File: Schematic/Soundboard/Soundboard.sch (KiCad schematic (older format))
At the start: 0 parts

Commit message: Begin rev 2 part selection and schematic
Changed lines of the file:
@@
 $Descr A4 11693 8268
 encoding utf-8
-Sheet 1 4
+Sheet 1 6
 Title ""
 Date ""
@@
 $EndSheet
 $Sheet
-S 4000 3200 1200 850
+S 4000 3050 1200 850
 U 5F0E4BAF
 F0 "Power" 50
 F1 "Power.sch" 50
 $EndSheet
+$Sheet
+S 1550 4800 1300 1150
+U 5F230DA4
+F0 "SDRAM" 50
+F1 "SDRAM.sch" 50
+$EndSheet
+$Sheet
+S 3400 4850 1300 1150
+U 5F230EC3
+F0 "Display" 50
+F1 "Display.sch" 50
+$EndSheet
 $EndSCHEMATC

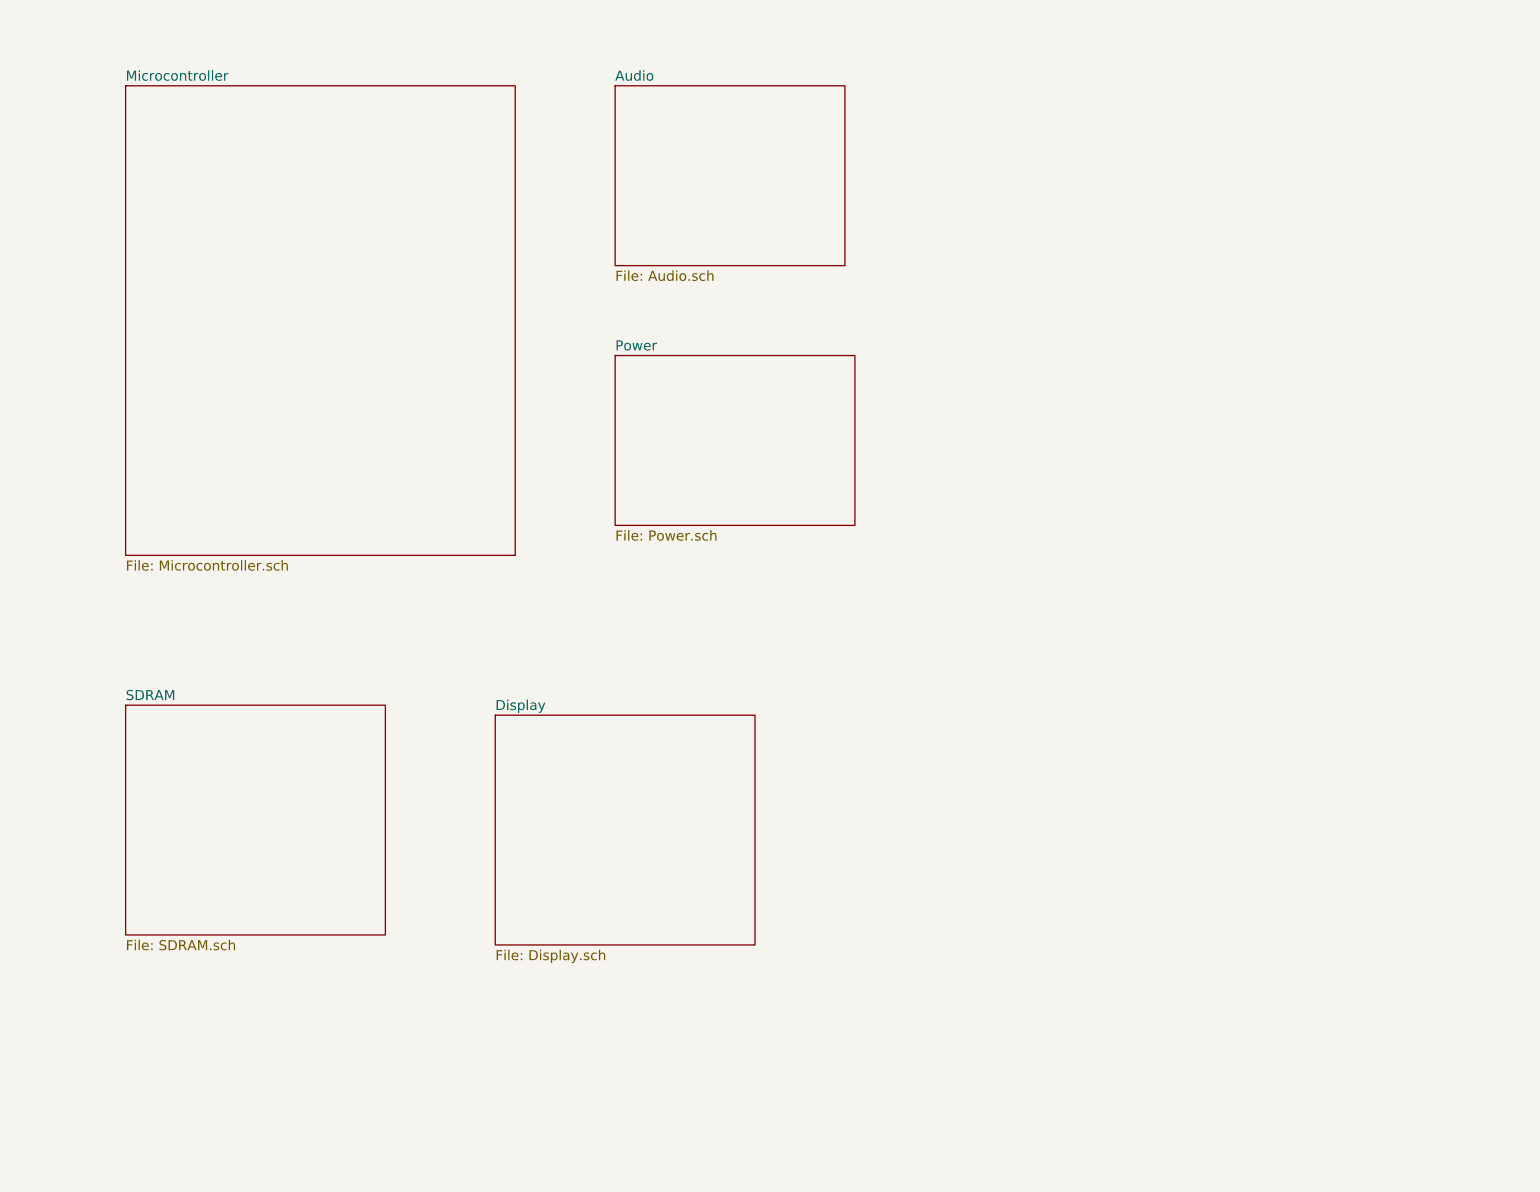
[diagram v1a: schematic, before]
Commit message: Complete part selection. Start connections
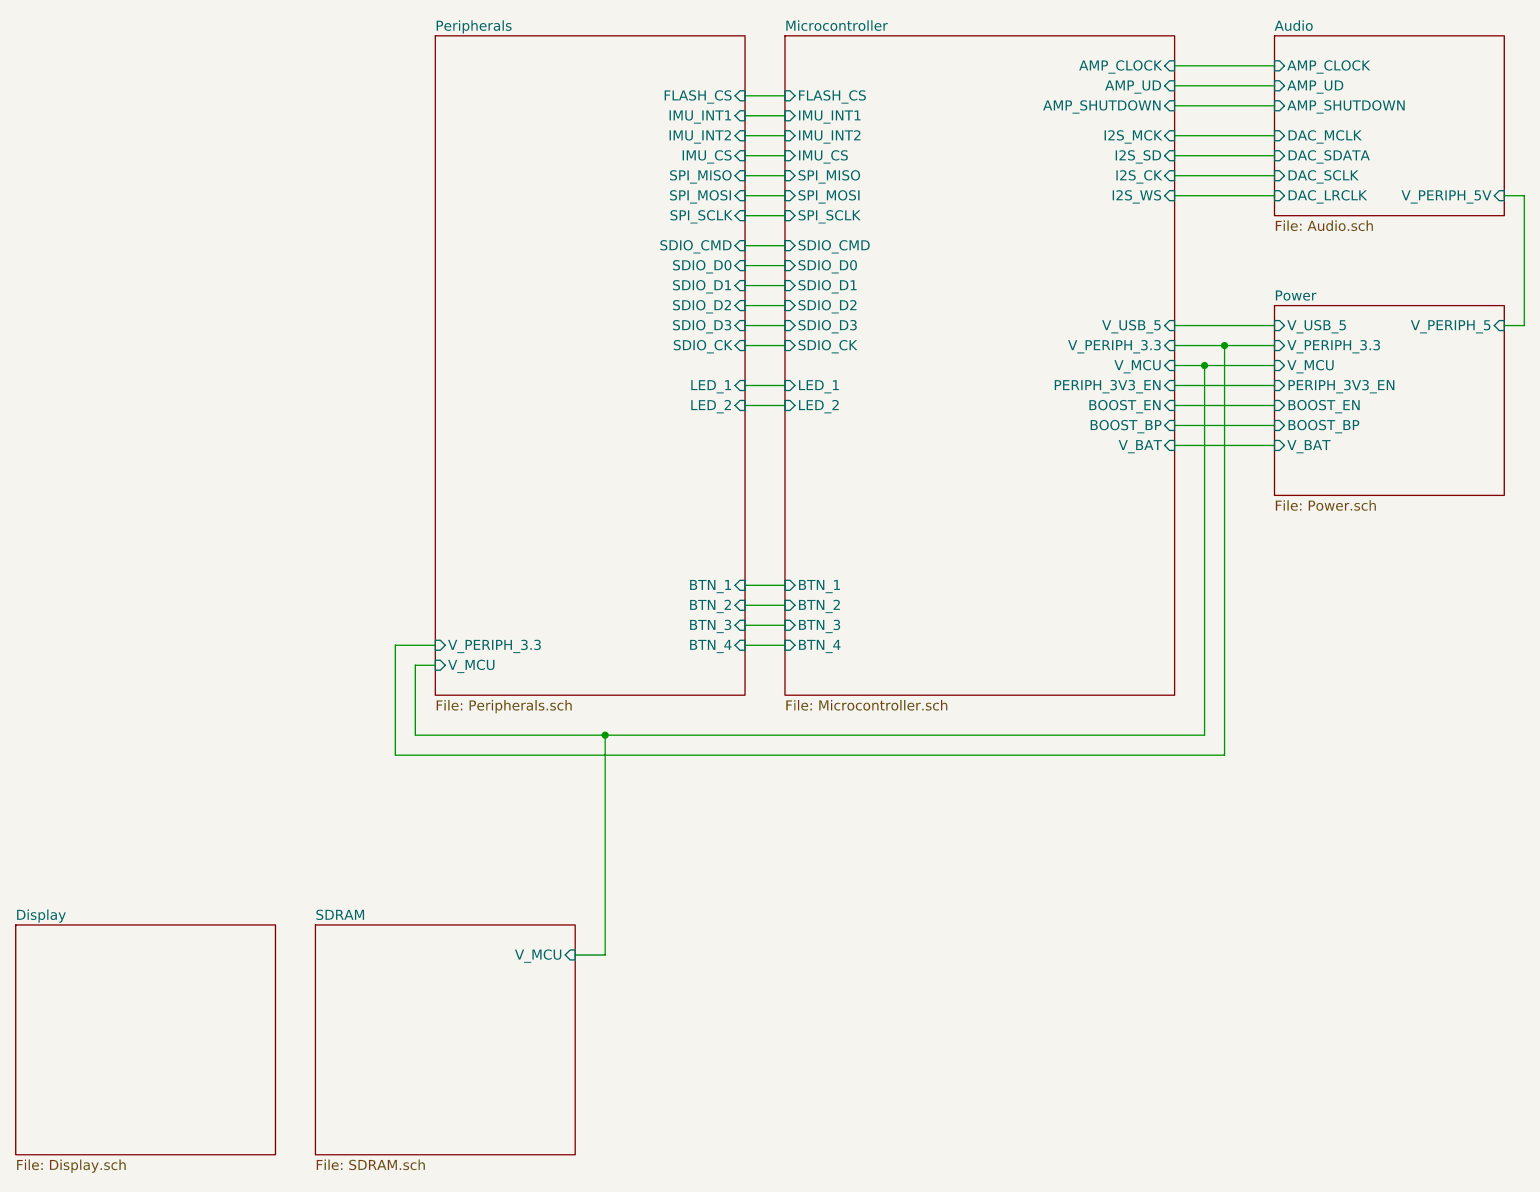
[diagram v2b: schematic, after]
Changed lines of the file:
@@
 EESchema Schematic File Version 4
-EELAYER 30 0
+LIBS:Soundboard-cache
+EELAYER 26 0
 EELAYER END
 $Descr A4 11693 8268
 encoding utf-8
-Sheet 1 6
+Sheet 1 7
 Title ""
 Date ""
@@
 $EndDescr
 $Sheet
-S 1550 1700 1950 2350
+S 7300 1450 1150 900
+U 5F0E03EF
+F0 "Audio" 50
+F1 "Audio.sch" 50
+F2 "V_PERIPH_5V" I R 8450 2250 50
+F3 "AMP_CLOCK" I L 7300 1600 50
+F4 "AMP_UD" I L 7300 1700 50
+F5 "AMP_SHUTDOWN" I L 7300 1800 50
+F6 "DAC_SDATA" I L 7300 2050 50
+F7 "DAC_SCLK" I L 7300 2150 50
+F8 "DAC_LRCLK" I L 7300 2250 50
+F9 "DAC_MCLK" I L 7300 1950 50
+$EndSheet
+$Sheet
+S 7300 2800 1150 950
+U 5F0E4BAF
+F0 "Power" 50
+F1 "Power.sch" 50
+F2 "V_USB_5" I L 7300 2900 50
+F3 "V_PERIPH_5" I R 8450 2900 50
+F4 "V_PERIPH_3.3" I L 7300 3000 50
+F5 "PERIPH_3V3_EN" I L 7300 3200 50
+F6 "BOOST_EN" I L 7300 3300 50
+F7 "BOOST_BP" I L 7300 3400 50
+F8 "V_MCU" I L 7300 3100 50
+F9 "V_BAT" I L 7300 3500 50
+$EndSheet
+$Sheet
+S 2500 5900 1300 1150
+U 5F230DA4
+F0 "SDRAM" 50
+F1 "SDRAM.sch" 50
+F2 "V_MCU" I R 3800 6050 50
+$EndSheet
+$Sheet
+S 1000 5900 1300 1150
+U 5F230EC3
+F0 "Display" 50
+F1 "Display.sch" 50
+$EndSheet
+Wire Wire Line
+	8550 2900 8550 2250
+Wire Wire Line
+	8550 2250 8450 2250
+Wire Wire Line
+	8450 2900 8550 2900
+$Sheet
+S 4850 1450 1950 3300
 U 5F0E03BF
 F0 "Microcontroller" 50
 F1 "Microcontroller.sch" 50
-$EndSheet
-$Sheet
-S 4000 1700 1150 900
-U 5F0E03EF
-F0 "Audio" 50
-F1 "Audio.sch" 50
-$EndSheet
-$Sheet
-S 4000 3050 1200 850
-U 5F0E4BAF
-F0 "Power" 50
-F1 "Power.sch" 50
-$EndSheet
-$Sheet
-S 1550 4800 1300 1150
-U 5F230DA4
-F0 "SDRAM" 50
-F1 "SDRAM.sch" 50
-$EndSheet
-$Sheet
-S 3400 4850 1300 1150
-U 5F230EC3
-F0 "Display" 50
-F1 "Display.sch" 50
-$EndSheet
+F2 "V_USB_5" I R 6800 2900 50
+F3 "V_PERIPH_3.3" I R 6800 3000 50
+F4 "V_MCU" I R 6800 3100 50
+F5 "BOOST_EN" I R 6800 3300 50
+F6 "BOOST_BP" I R 6800 3400 50
+F7 "PERIPH_3V3_EN" I R 6800 3200 50
+F8 "AMP_CLOCK" I R 6800 1600 50
+F9 "AMP_UD" I R 6800 1700 50
+F10 "AMP_SHUTDOWN" I R 6800 1800 50
+F11 "I2S_SD" I R 6800 2050 50
+F12 "I2S_WS" I R 6800 2250 50
+F13 "I2S_CK" I R 6800 2150 50
+F14 "I2S_MCK" I R 6800 1950 50
+F15 "IMU_INT1" I L 4850 1850 50
+F16 "IMU_INT2" I L 4850 1950 50
+F17 "IMU_CS" I L 4850 2050 50
+F18 "SPI_MISO" I L 4850 2150 50
+F19 "SPI_MOSI" I L 4850 2250 50
+F20 "SPI_SCLK" I L 4850 2350 50
+F21 "FLASH_CS" I L 4850 1750 50
+F22 "SDIO_D0" I L 4850 2600 50
+F23 "SDIO_D1" I L 4850 2700 50
+F24 "SDIO_D2" I L 4850 2800 50
+F25 "SDIO_D3" I L 4850 2900 50
+F26 "SDIO_CK" I L 4850 3000 50
+F27 "LED_1" I L 4850 3200 50
+F28 "LED_2" I L 4850 3300 50
+F29 "SDIO_CMD" I L 4850 2500 50
+F30 "BTN_1" I L 4850 4200 50
+F31 "BTN_2" I L 4850 4300 50
+F32 "BTN_3" I L 4850 4400 50
+F33 "BTN_4" I L 4850 4500 50
+F34 "V_BAT" I R 6800 3500 50
+$EndSheet
+Wire Wire Line
+	6800 1950 7300 1950
+Wire Wire Line
+	6800 2050 7300 2050
+Wire Wire Line
+	6800 2150 7300 2150
+Wire Wire Line
+	6800 2250 7300 2250
+Wire Wire Line
+	6800 1800 7300 1800
+Wire Wire Line
+	6800 1700 7300 1700
+Wire Wire Line
+	6800 1600 7300 1600
+Wire Wire Line
+	6800 2900 7300 2900
+Wire Wire Line
+	6800 3000 7050 3000
+Wire Wire Line
+	6800 3100 6950 3100
+Wire Wire Line
+	6800 3200 7300 3200
+Wire Wire Line
+	6800 3300 7300 3300
+Wire Wire Line
+	6800 3400 7300 3400
+$Sheet
+S 3100 1450 1550 3300
+U 5F4E88D1
+F0 "Peripherals" 50
+F1 "Peripherals.sch" 50
+F2 "V_PERIPH_3.3" I L 3100 4500 50
+F3 "V_MCU" I L 3100 4600 50
+F4 "IMU_INT1" I R 4650 1850 50
+F5 "IMU_INT2" I R 4650 1950 50
+F6 "IMU_CS" I R 4650 2050 50
+F7 "SPI_MISO" I R 4650 2150 50
+F8 "SPI_MOSI" I R 4650 2250 50
+F9 "SPI_SCLK" I R 4650 2350 50
+F10 "FLASH_CS" I R 4650 1750 50
+F11 "LED_1" I R 4650 3200 50
+F12 "LED_2" I R 4650 3300 50
+F13 "BTN_1" I R 4650 4200 50
+F14 "BTN_2" I R 4650 4300 50
+F15 "BTN_3" I R 4650 4400 50
+F16 "BTN_4" I R 4650 4500 50
+F17 "SDIO_D3" I R 4650 2900 50
+F18 "SDIO_D0" I R 4650 2600 50
+F19 "SDIO_D1" I R 4650 2700 50
+F20 "SDIO_D2" I R 4650 2800 50
+F21 "SDIO_CK" I R 4650 3000 50
+F22 "SDIO_CMD" I R 4650 2500 50
+$EndSheet
+Wire Wire Line
+	4650 4200 4850 4200
+Wire Wire Line
+	4650 4300 4850 4300
+Wire Wire Line
+	4650 4400 4850 4400
+Wire Wire Line
+	4650 4500 4850 4500
+Wire Wire Line
+	4650 3300 4850 3300
+Wire Wire Line
+	4650 3200 4850 3200
+Wire Wire Line
+	4650 3000 4850 3000
+Wire Wire Line
+	4650 2900 4850 2900
+Wire Wire Line
+	4650 2800 4850 2800
+Wire Wire Line
+	4650 2700 4850 2700
+Wire Wire Line
+	4650 2600 4850 2600
+Wire Wire Line
+	4650 2500 4850 2500
+Wire Wire Line
+	4650 2350 4850 2350
+Wire Wire Line
+	4650 2250 4850 2250
+Wire Wire Line
+	4650 2150 4850 2150
+Wire Wire Line
+	4650 2050 4850 2050
+Wire Wire Line
+	4650 1950 4850 1950
+Wire Wire Line
+	4650 1850 4850 1850
+Wire Wire Line
+	4650 1750 4850 1750
+Wire Wire Line
+	6950 3100 6950 4950
+Wire Wire Line
+	6950 4950 3950 4950
+Connection ~ 6950 3100
+Wire Wire Line
+	6950 3100 7300 3100
+Wire Wire Line
+	7050 3000 7050 5050
+Wire Wire Line
+	7050 5050 2900 5050
+Connection ~ 7050 3000
+Wire Wire Line
+	7050 3000 7300 3000
+Wire Wire Line
+	3000 4950 3000 4600
+Wire Wire Line
+	3000 4600 3100 4600
+Wire Wire Line
+	2900 5050 2900 4500
+Wire Wire Line
+	2900 4500 3100 4500
+Wire Wire Line
+	3950 4950 3950 6050
+Wire Wire Line
+	3950 6050 3800 6050
+Connection ~ 3950 4950
+Wire Wire Line
+	3950 4950 3000 4950
+Wire Wire Line
+	6800 3500 7300 3500
 $EndSCHEMATC
